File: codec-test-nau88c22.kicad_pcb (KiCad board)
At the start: 2 copper layers, 100 x 100 mm, 74 parts, among them J1 Conn_01x03_Male, J10 AudioJack3, J11 Conn_01x02_Male, J2 Conn_01x03_Male, J3 Conn_02x05_Odd_Even, J4 Conn_02x04_Odd_Even, J5 AudioJack3, J6 AudioJack3, J7 AudioJack3, J8 AudioJack2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

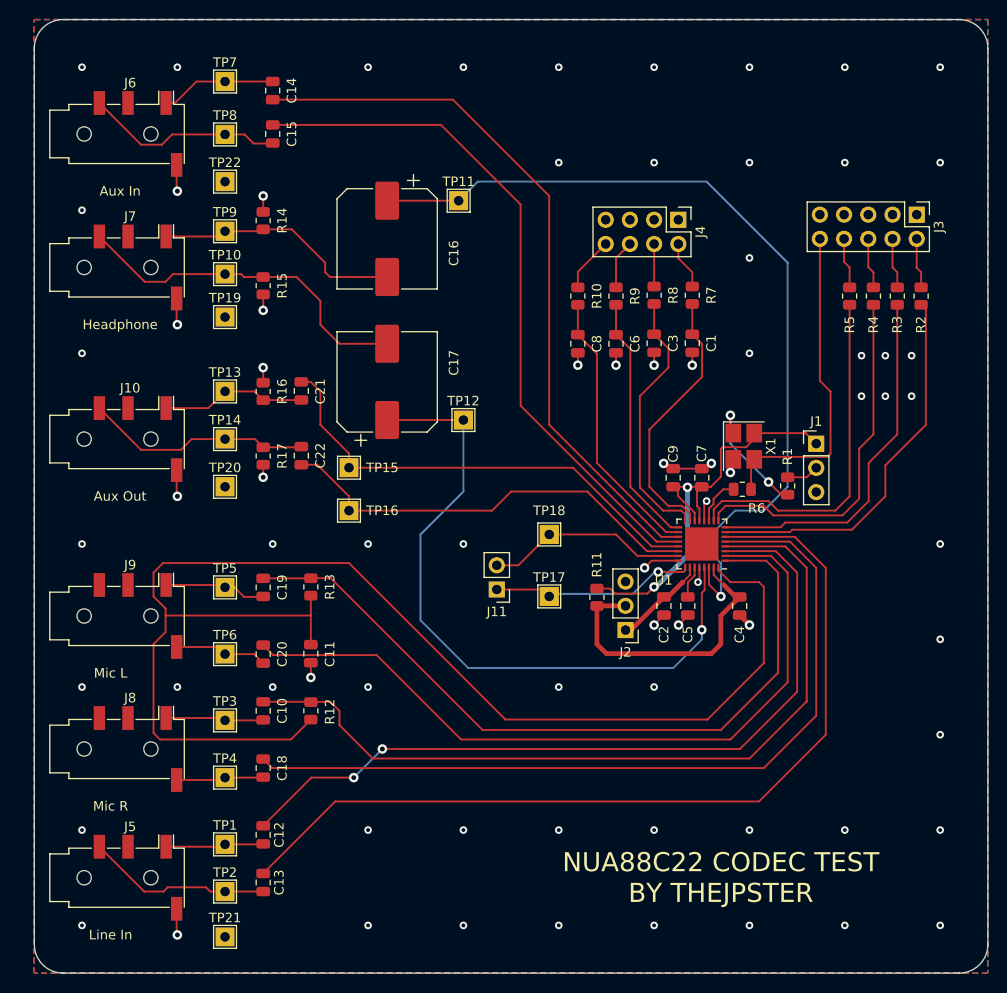
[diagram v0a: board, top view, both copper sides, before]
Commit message: Rewired then updated kibot
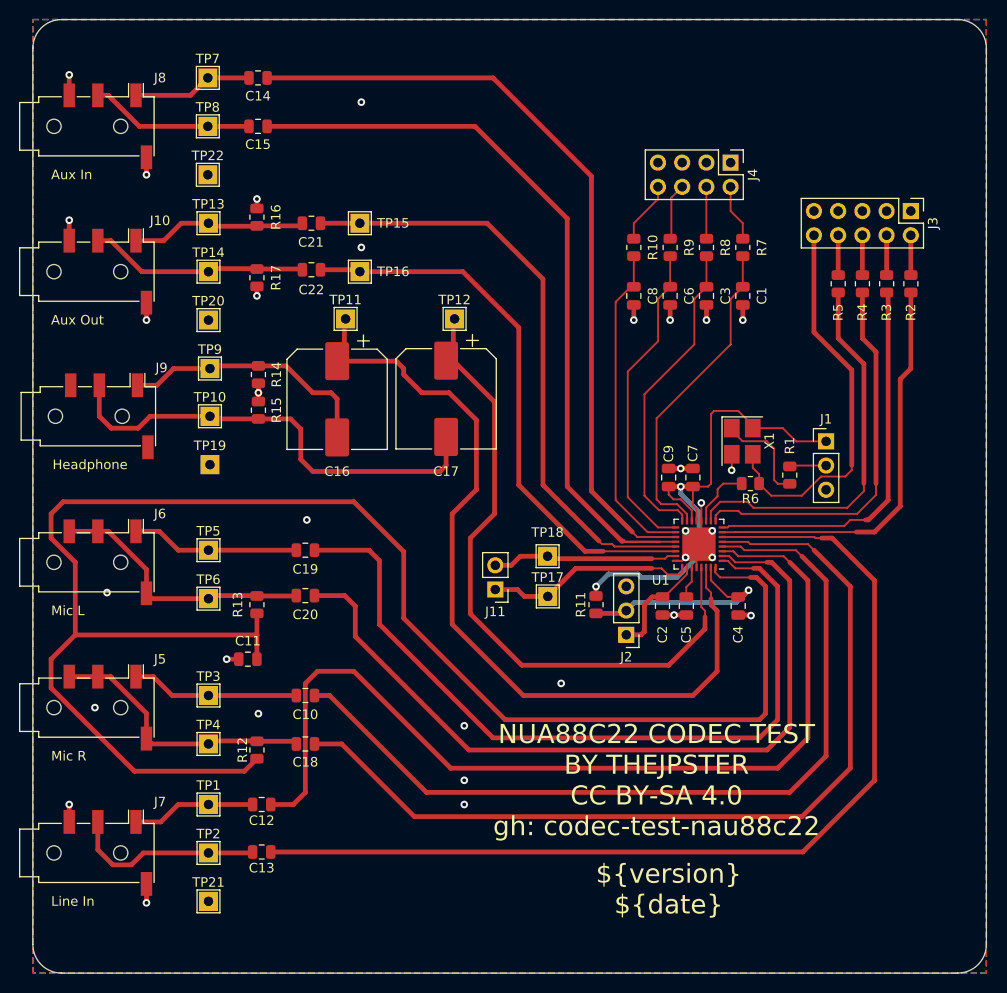
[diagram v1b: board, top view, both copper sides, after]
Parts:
- removed TP19: TestPoint, TestPoint:TestPoint_THTPad_2.0x2.0mm_Drill1.0mm
- added ?: , , F.Cu at (58.4, 111.7)
- J10, J5, J6, J7: value AudioJack3 -> AudioJack4
- J8, J9: value AudioJack2 -> AudioJack4
- moved J8 65.4 mm to (46.8, 76.2)
- moved J7 61.5 mm to (46.8, 152.4)
- moved J6 45.0 mm to (46.8, 121.9)
- moved TP15 25.7 mm to (74.1, 86.4)
- moved TP16 25.1 mm to (74.1, 91.4)
- moved J9 21.2 mm to (47.0, 106.6)
- moved C22 19.5 mm to (69.1, 91.2), turned to 180 degrees
- moved R17 18.7 mm to (63.3, 92.1)
- moved R16 18.3 mm to (63.3, 85.7)
- moved J5 18.1 mm to (46.8, 137.2)
- moved J10 17.8 mm to (46.8, 91.4)
- moved TP13 17.7 mm to (58.3, 86.4)
- moved TP14 17.6 mm to (58.3, 91.4)
- moved C16 17.6 mm to (71.8, 104.8)
- moved C21 17.6 mm to (69.1, 86.4), turned to 180 degrees
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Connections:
- J10 pad R1: (no net) -> /AUXOUT2
- J5 pad R1: (no net) -> /RM-
- J5 pad S: GND -> /RM-
- J5 pad T: /LLIN -> /RM+
- J6 pad R1: (no net) -> /LM-
- J6 pad S: GND -> /LM-
- J6 pad T: /LAUXIN -> /LM+
- J7 pad R1: (no net) -> /RLIN
- J7 pad T: /LHP -> /LLIN
- J8 pad R1: (no net) -> /RAUXIN
- J8 pad S: /RM- -> GND
- J8 pad T: /RM+ -> /LAUXIN
- J9 pad R1: (no net) -> /RHP
- J9 pad R2: (no net) -> GND
- J9 pad S: /LM- -> GND
- J9 pad T: /LM+ -> /LHP
- R12 pad 1: /RMDC+ -> /RM-
- R13 pad 1: /LMDC+ -> /LM-
- U1 pad 33: (no net) -> GND
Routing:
- net /MICBIAS: track 143.3 -> 179.1 mm
- net /RM-: track 8.78 -> 28.1 mm
- net /LM-: track 8.72 -> 27.6 mm
- net /LLIN_DC: track 82.8 -> 101.1 mm, vias 2 -> 0
- net /AUXOUT1_DC: track 49.6 -> 64.4 mm
- net /AUXOUT2_DC: track 45.8 -> 58.9 mm
- net /RLIN_DC: track 94.4 -> 105.2 mm
- net /RHP: track 37.0 -> 47.8 mm
- net +3.3V: track 46.5 -> 55.6 mm
- net /RMDC-: track 86.9 -> 95.9 mm
- net +3.3VA: track 31.1 -> 22.5 mm, vias 0 -> 1
- net /RAUXIN_DC: track 73.0 -> 81.4 mm
- net /RM+: track 9.88 -> 17.6 mm
- net /LM+: track 10.3 -> 17.6 mm
- net Net-(J3-Pad10): track 33.7 -> 41.0 mm
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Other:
- board text added: "${version} ${date}"
- board text added: "NUA88C22 CODEC TEST BY THEJPSTER CC BY-SA 4.0 gh: codec-test-nau88c22"
- board text added: "TP19"
- board text removed: "NUA88C22 CODEC TEST BY THEJPSTER"

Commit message: Fix DRC errors
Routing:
- net GND: vias 33 -> 65
